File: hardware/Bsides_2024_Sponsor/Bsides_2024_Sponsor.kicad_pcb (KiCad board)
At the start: 2 copper layers, 139.6 x 139.6 mm, 45 parts, among them J1 Serial_IN, J2 Add_On, J3 OLED, J4 Serial_OUT, J5 Battery, J6 Battery, P1 USB_C_Plug_USB2.0, Q1 DMG3415U-7, SW1 ON, SW2 RESET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

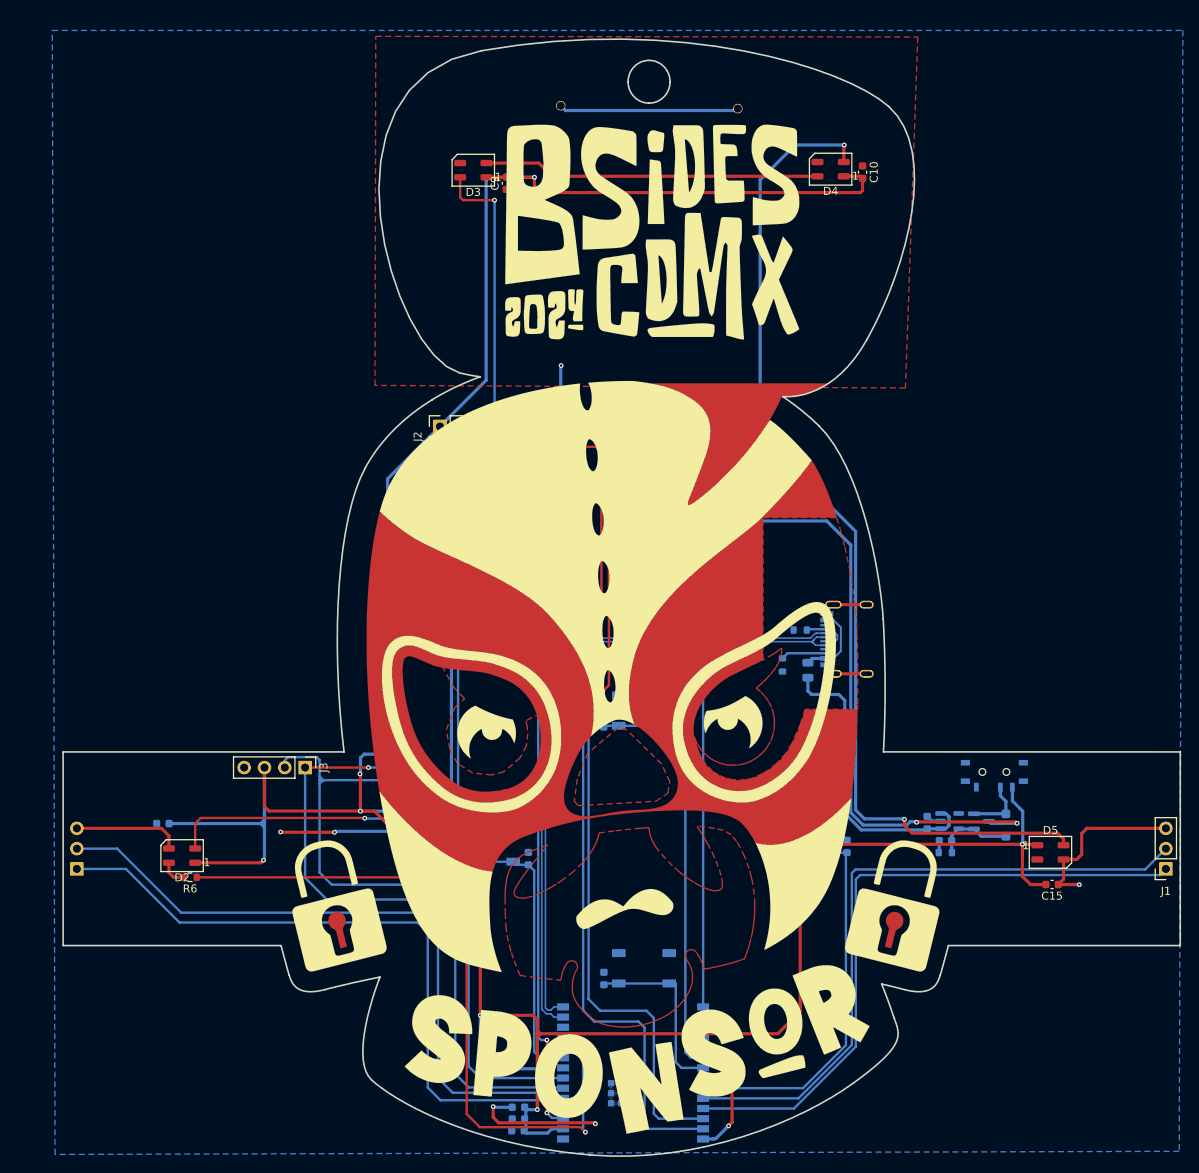
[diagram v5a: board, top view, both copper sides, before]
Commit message: fet(Hw): Update route
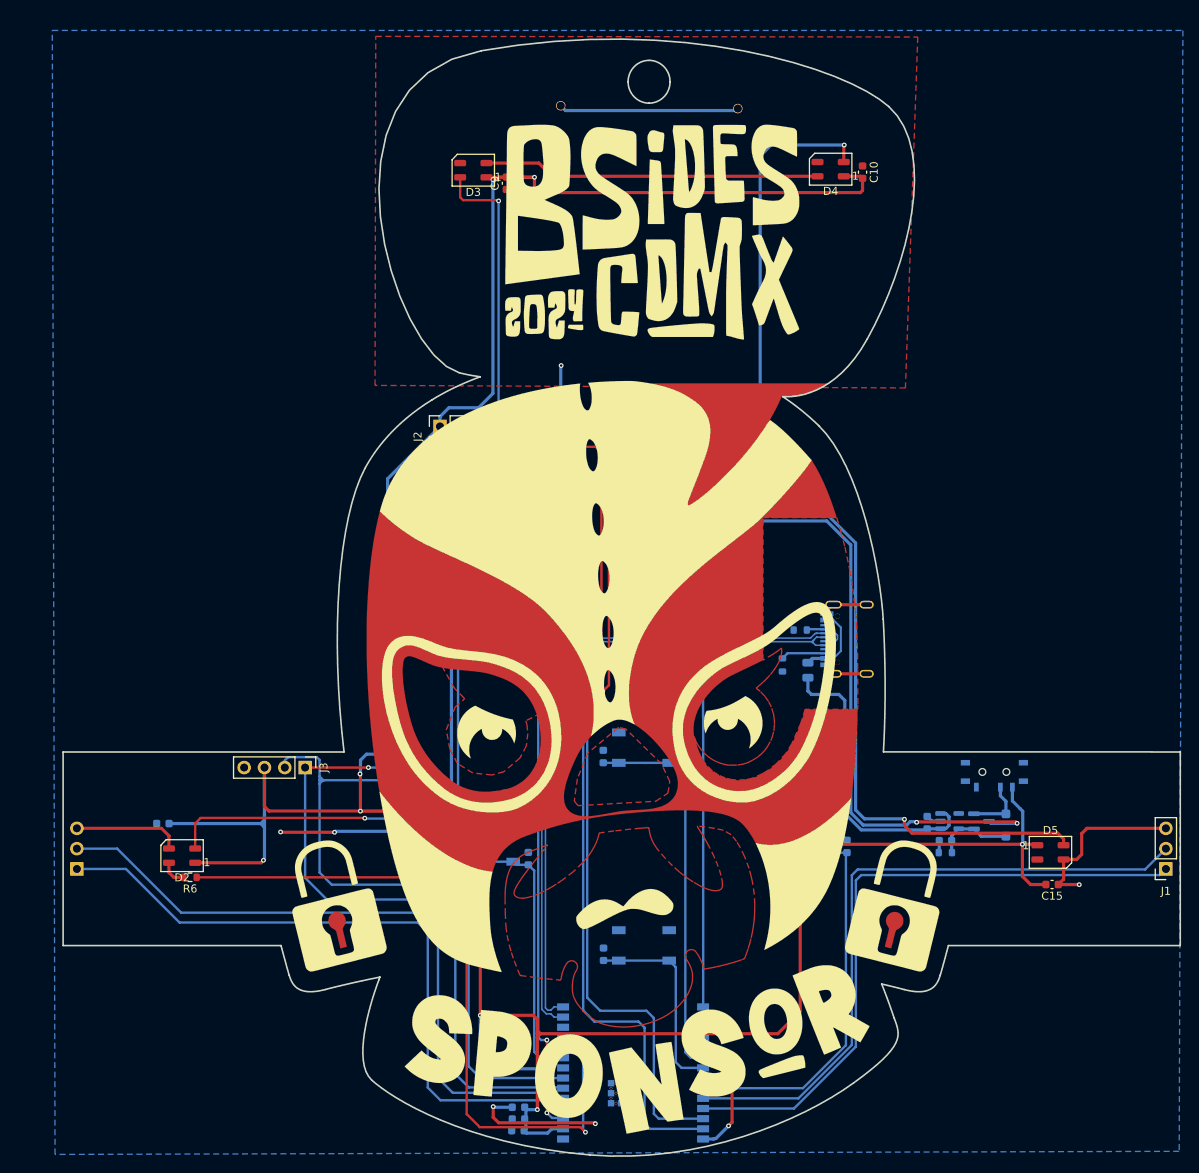
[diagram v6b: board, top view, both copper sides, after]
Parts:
- added kibuzzard-666A0720: G***, kibuzzard-666A0720, B.Cu at (163.2, 117.9)
- moved SW6 4.63 mm to (145.7, 111.3)
- moved C13 4.45 mm to (140.6, 112.4)
- moved C14 3.03 mm to (140.7, 137.1)
- moved SW7 2.86 mm to (145.7, 136.0)
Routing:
- net Net-(D4-DOUT): track 126.9 -> 132.8 mm
- net /GPIO22: track 52.8 -> 48.5 mm
- net /GPIO23: track 22.6 -> 25.0 mm
- net /VOUT: track 402.0 -> 404.4 mm
- net /PIN: track 90.1 -> 91.2 mm
- net Net-(D2-DOUT): track 129.0 -> 129.7 mm

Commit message: feat(Hw): Update route Speaker and Sponsor
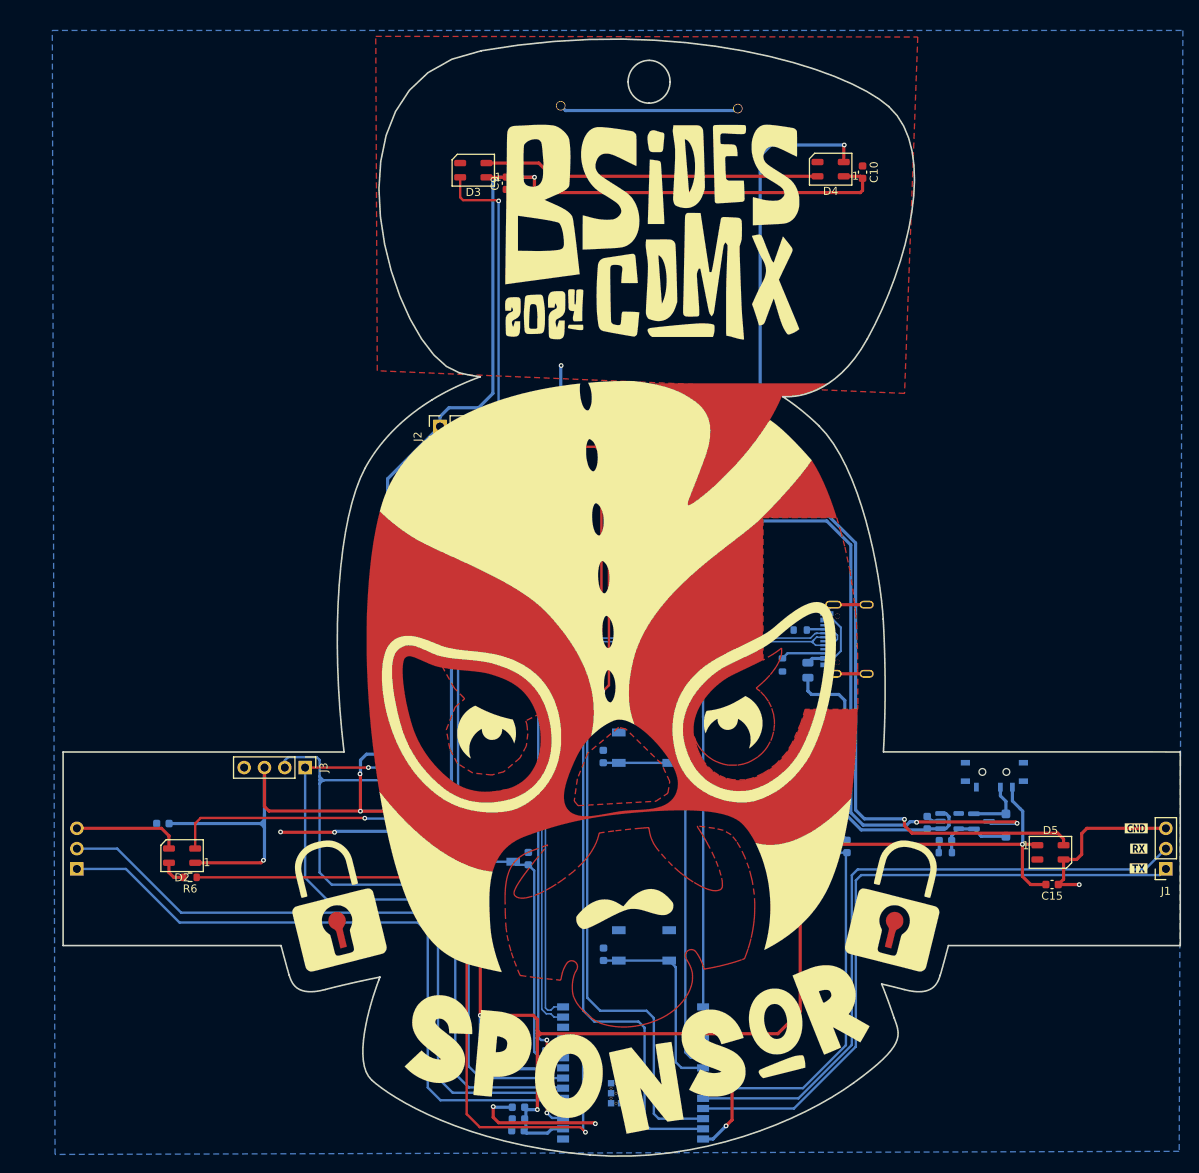
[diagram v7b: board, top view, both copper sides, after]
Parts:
- removed kibuzzard-666A0720: G***, kibuzzard-666A0720
- added kibuzzard-666B3243: G***, kibuzzard-666B3243, B.Cu at (145.7, 115.0)
- added kibuzzard-666B3258: G***, kibuzzard-666B3258, B.Cu at (145.7, 132.3)
- added kibuzzard-666B327A: G***, kibuzzard-666B327A, B.Cu at (134.0, 123.2)
- added kibuzzard-666B55CA: G***, kibuzzard-666B55CA, B.Cu at (158.1, 123.5)
- added kibuzzard-666B5A62: G***, kibuzzard-666B5A62, F.Cu at (207.6, 126.4)
- added kibuzzard-666B5A62: G***, kibuzzard-666B5A62, B.Cu at (78.2, 123.9)
- added kibuzzard-666B5A91: G***, kibuzzard-666B5A91, F.Cu at (207.6, 123.9)
- added kibuzzard-666B5A91: G***, kibuzzard-666B5A91, B.Cu at (78.1, 126.4)
- added kibuzzard-666B5AA1: G***, kibuzzard-666B5AA1, F.Cu at (207.3, 121.4)
- added kibuzzard-666B5AA1: G***, kibuzzard-666B5AA1, B.Cu at (78.5, 121.4)
- added kibuzzard-666B5BCA: G***, kibuzzard-666B5BCA, B.Cu at (120.2, 68.7)
- added kibuzzard-666B5C0A: G***, kibuzzard-666B5C0A, B.Cu at (120.3, 76.1)
- added kibuzzard-666B5C24: G***, kibuzzard-666B5C24, B.Cu at (122.8, 68.2)
- added kibuzzard-666B5C33: G***, kibuzzard-666B5C33, B.Cu at (122.8, 76.5)
- F1: value 0.5A -> 0.75A
- moved R1 0.39 mm to (133.5, 149.9)
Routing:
- net /BOOT: track 95.5 -> 93.7 mm

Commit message: feat(Hw): Update labels
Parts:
- added kibuzzard-666B5BCA: G***, kibuzzard-666B5BCA, B.Cu at (135.4, 33.1)
- added kibuzzard-666B5BCA: G***, kibuzzard-666B5BCA, B.Cu at (157.4, 80.8)
- added kibuzzard-666B5C0A: G***, kibuzzard-666B5C0A, B.Cu at (157.5, 33.3)
- added kibuzzard-666B5C0A: G***, kibuzzard-666B5C0A, B.Cu at (135.3, 80.6)
- added kibuzzard-666C631C: G***, kibuzzard-666C631C, B.Cu at (115.6, 83.4)
- added kibuzzard-666C633C: G***, kibuzzard-666C633C, B.Cu at (115.7, 92.8)
- added kibuzzard-666C639C: G***, kibuzzard-666C639C, B.Cu at (194.4, 117.2)
- added kibuzzard-666C63C4: G***, kibuzzard-666C63C4, B.Cu at (184.6, 117.2)
